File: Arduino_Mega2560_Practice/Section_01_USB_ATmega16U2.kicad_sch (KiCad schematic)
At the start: 1 part, among them J1 USB_C_Receptacle_USB2.0_16P

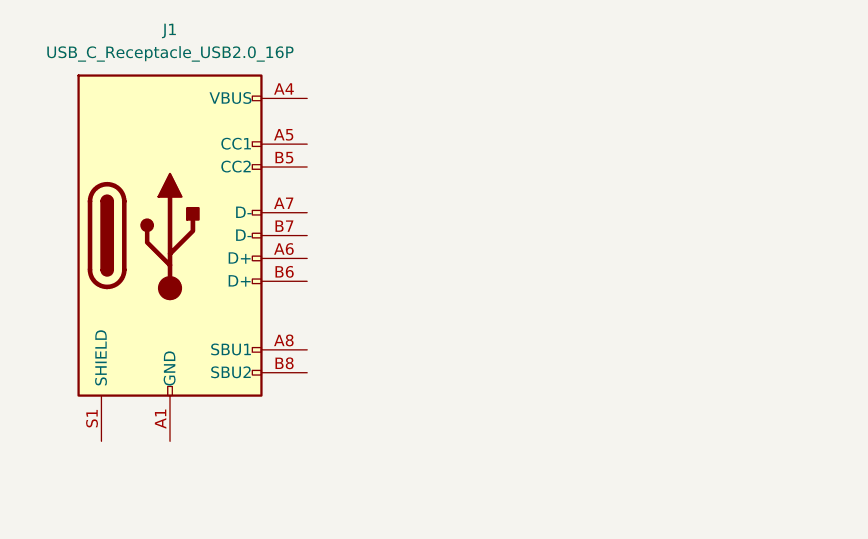
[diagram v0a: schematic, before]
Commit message: add resistor R1-R5
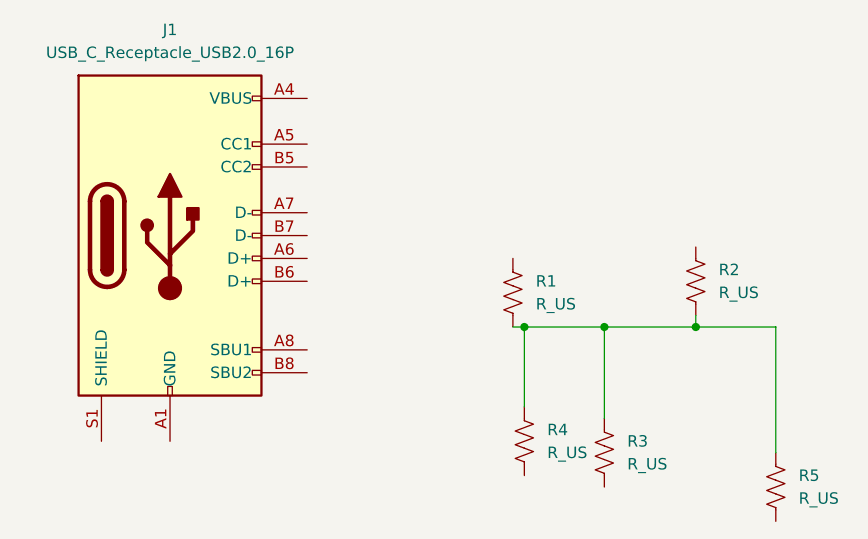
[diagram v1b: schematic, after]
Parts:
- added R1, R2, R3, R4, R5: R_US, symbol Device:R_US
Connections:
- new net: R1.2, R2.2, R3.1, R4.1, R5.1
